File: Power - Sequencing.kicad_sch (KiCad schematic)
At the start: 0 parts

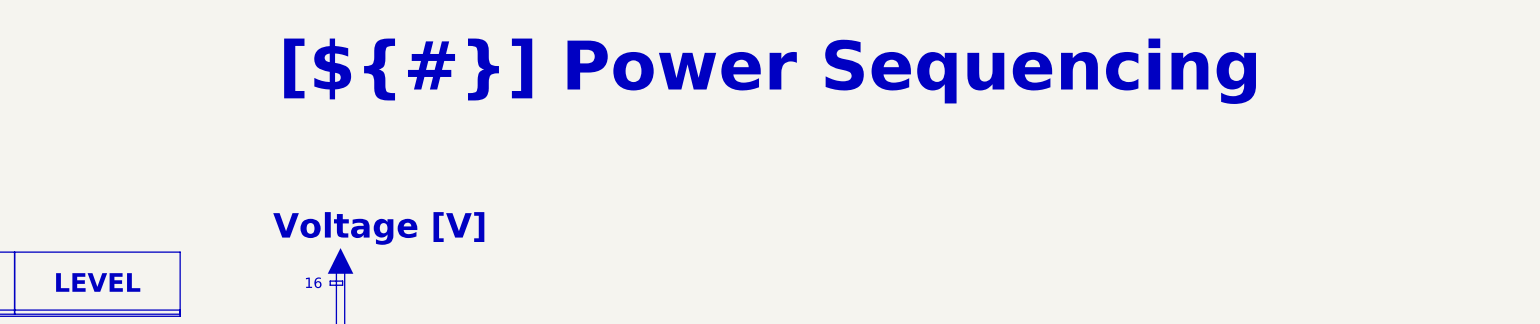
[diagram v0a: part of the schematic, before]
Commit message: [Project][Added] CI/CD environment
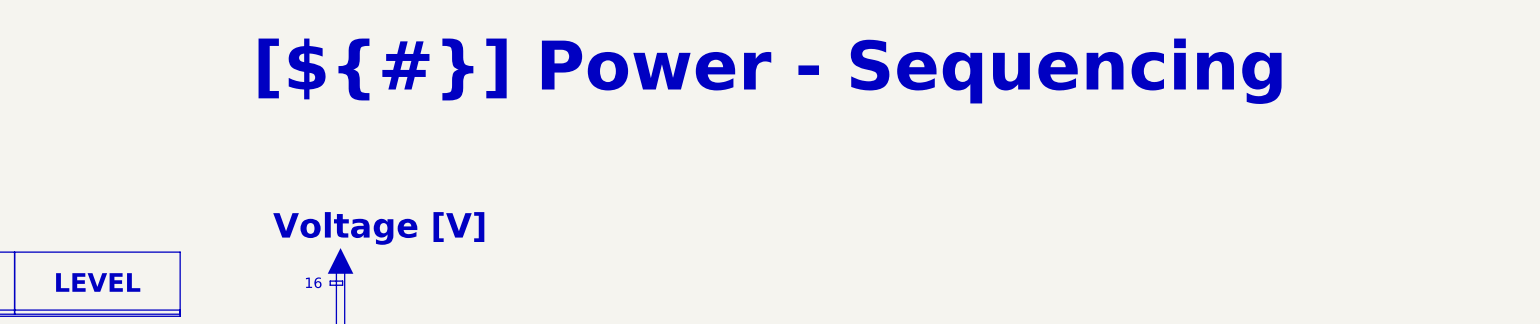
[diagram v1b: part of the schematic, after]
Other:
- title: Power Sequencing -> Power - Sequencing
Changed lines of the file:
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@@
 (kicad_sch
-	(version 20260306)
+	(version 20250114)
 	(generator "eeschema")
-	(generator_version "10.0")
+	(generator_version "9.0")
 	(paper "A4")
 	(title_block
-		(title "Power Sequencing")
+		(title "Power - Sequencing")
 		(date "2025-01-12")
 		(rev "${REVISION}")
